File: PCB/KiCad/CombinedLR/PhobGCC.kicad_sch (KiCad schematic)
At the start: 66 parts, among them J1 Conn_01x06_Female, J2 Conn_01x04_Female, J3 Conn_01x01_Male, J5 Conn_01x02_Male, Q1 Q_NMOS_GSD, Q2 Q_PMOS_GDS, Q3 Q_NMOS_GSD, SW1 A, SW10 Dup, SW11 Dright, SW12 Ddown, SW2 B, SW3 X, SW4 Y, SW5 Start, SW6 L, SW7 R, SW9 Dleft, U1 Teensy4.0, U2 2x DRV5053CAQLPGM Hall Effect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, U3 GP2S60-MFG, U4 GP2S60-MFG

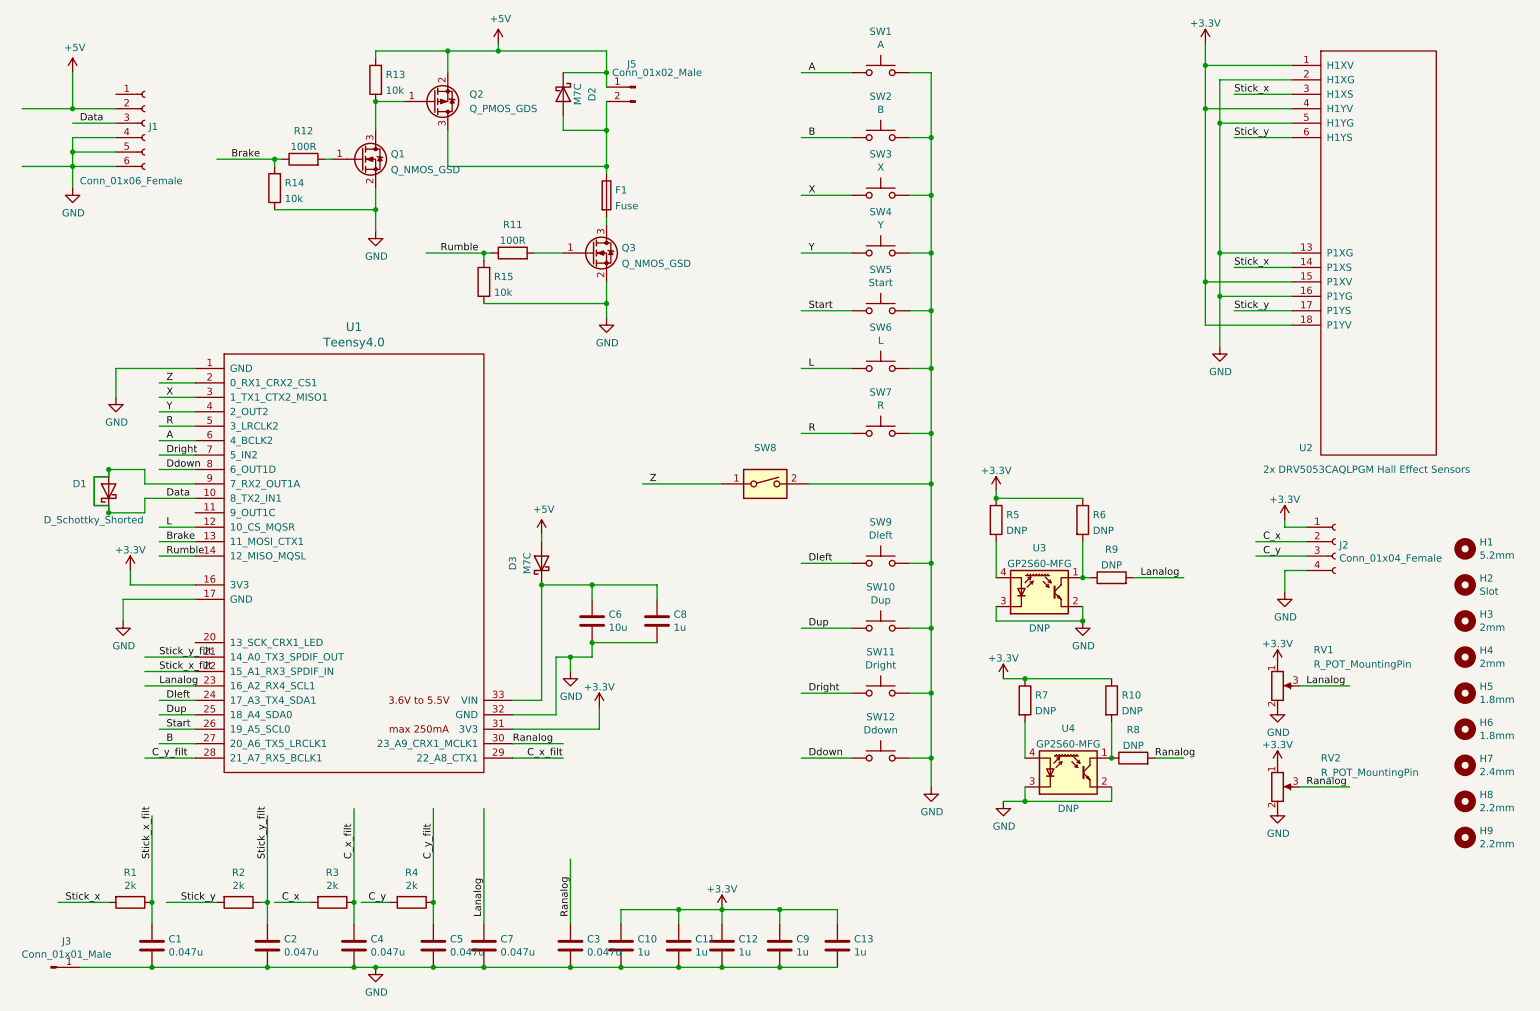
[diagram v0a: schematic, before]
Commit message: Updates
- switched rumble pads to SMD and matched OEM placement.
- aligned both sets of trigger pads to be horizontal for convenience and consistency.
- centered c-stick pins to the board edge.
- rerouted some areas to have a more consistent copper fill.
- fixed trigger board width (switched 7.5mm to 7.35mm).
- increased dpad button pad size to make for easier hand soldering.
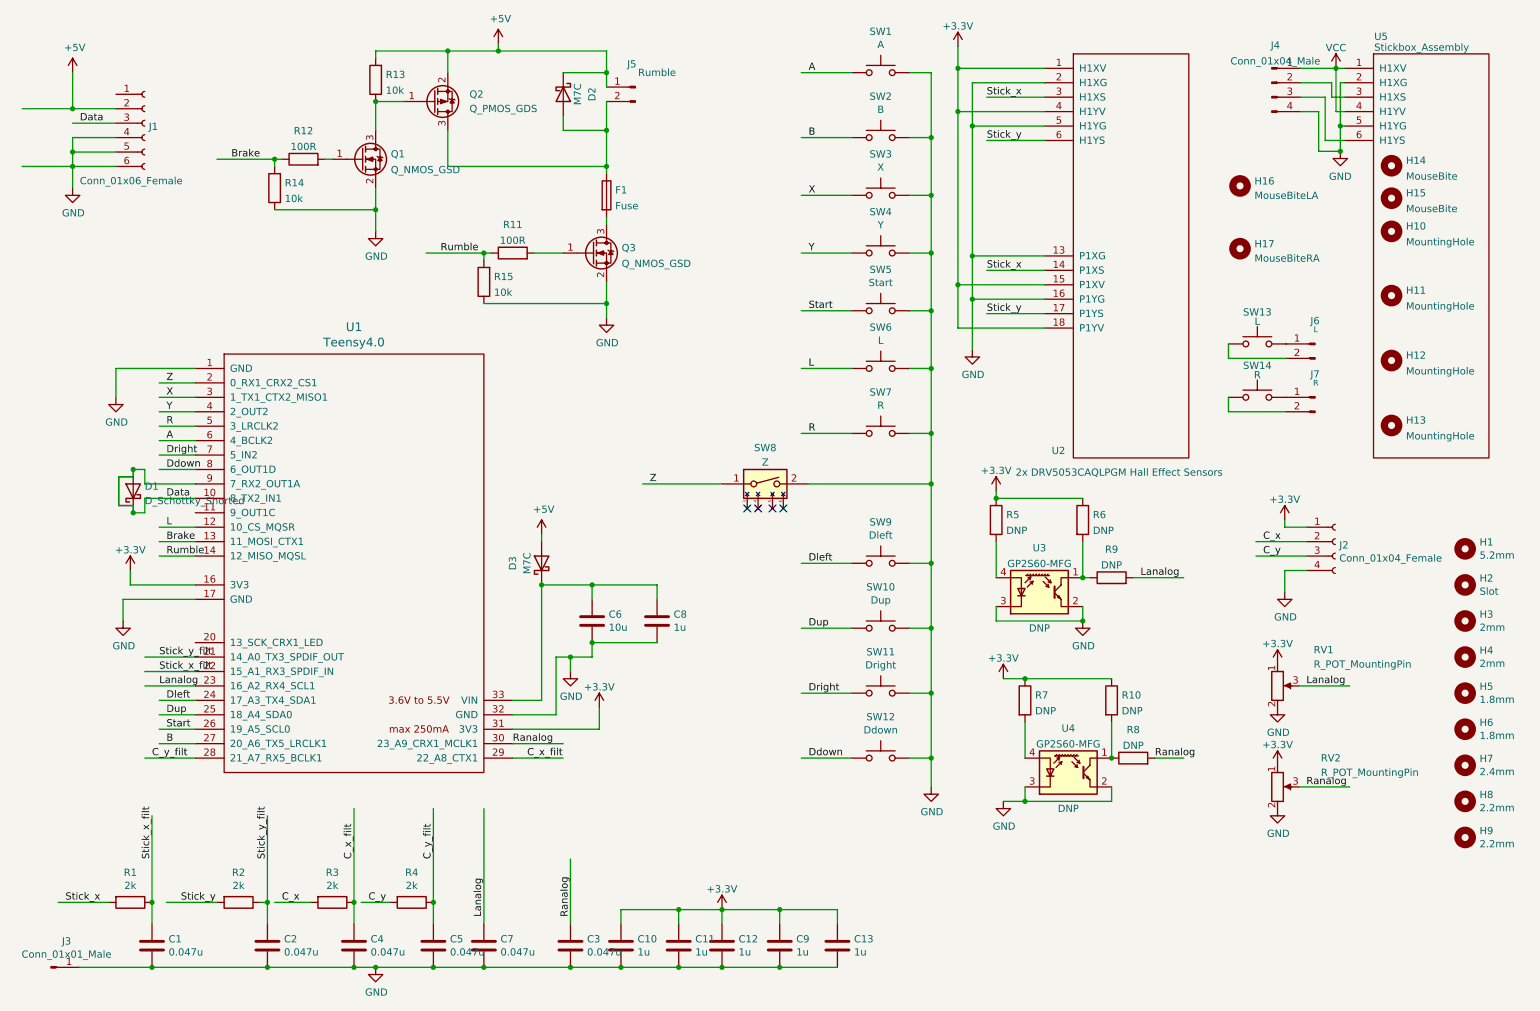
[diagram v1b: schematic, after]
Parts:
- removed D1: D_Schottky_Shorted, PhobGCC_Footprints:D_SOD-523_Shorted, symbol Gamecube MB:D_Schottky_Shorted
- added D1: D_Schottky_Shorted, wavbrd:D_SOD-523_Shorted, symbol PhobGCC_Symbol_Library:D_Schottky_Shorted
- added H10: MountingHole, PhobGCC_Footprints:MountingHole_1.8mm, symbol Mechanical:MountingHole
- added H11: MountingHole, PhobGCC_Footprints:MountingHole_5.2mm, symbol Mechanical:MountingHole
- added H12, H13: MountingHole, PhobGCC_Footprints:MountingHole_2.0mm, symbol Mechanical:MountingHole
- added H14, H15: MouseBite, PhobGCC_Footprints:breakaway-mousebites-double, symbol Mechanical:MountingHole
- added H16: MouseBiteLA, PhobGCC_Footprints:breakaway-mousebites-double, symbol Mechanical:MountingHole
- added H17: MouseBiteRA, PhobGCC_Footprints:breakaway-mousebites-double, symbol Mechanical:MountingHole
- added J4: Conn_01x04_Male, Connector_PinHeader_2.00mm:PinHeader_1x04_P2.00mm_Vertical, symbol Connector:Conn_01x04_Male
- added J6: L, PhobGCC_Footprints:Pin_Header_Straight_1x02_Pitch2.54mm, symbol Connector:Conn_01x02_Male
- added J7: R, PhobGCC_Footprints:Pin_Header_Straight_1x02_Pitch2.54mm, symbol Connector:Conn_01x02_Male
- added SW13: L, PhobGCC_Footprints:Trigger_Contact, symbol Switch:SW_Push
- added SW14: R, PhobGCC_Footprints:Trigger_Contact, symbol Switch:SW_Push
- added U5: Stickbox_Assembly, PhobGCC_Footprints:GCC_Stickbox_Hall_Only, symbol Gamecube MB:Stickbox_Assembly_Hall_Only
- J5: value Conn_01x02_Male -> Rumble; footprint PhobGCC_Footprints:Pin_Header_Straight_1x02_Pitch2.54mm -> (none)
- SW8: value (none) -> Z; symbol Switch:SW_DIP_x01 -> PhobGCC_Symbol_Library:SW_DIP_x01
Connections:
- net Data: now also D1.1 (K), D1.2 (A)
- net GND: now also J4.4 (Pin_4), U5.2 (H1XG), U5.5 (H1YG)
- new net: J6.1 (Pin_1), SW13.1
- new net: J6.2 (Pin_2), SW13.2
- new net: J7.1 (Pin_1), SW14.1
- new net: J7.2 (Pin_2), SW14.2
- new net: J4.2 (Pin_2), U5.3 (H1XS)
- new net: J4.3 (Pin_3), U5.6 (H1YS)
- new net VCC: J4.1 (Pin_1), U5.1 (H1XV), U5.4 (H1YV)
- no-connect marks 0 -> 4
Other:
- moved on the sheet: U2

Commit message: Consolidated footprints to PhobGCC library
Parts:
- C1, C2, C3, C4, C5, C6, C7: footprint Capacitors_SMD:C_0603_HandSoldering -> (none)
- C10, C11, C12, C13, C8, C9: footprint Capacitor_SMD:C_0603_1608Metric_Pad1.08x0.95mm_HandSolder -> (none)
- D1: footprint wavbrd:D_SOD-523_Shorted -> (none)
- D2, D3: footprint Diode_SMD:D_SOD-123 -> (none)
- F1: footprint Resistor_SMD:R_1206_3216Metric -> (none)
- J2: footprint Pin_Headers:Pin_Header_Straight_1x04_Pitch2.00mm -> (none)
- J3: footprint Connector_PinHeader_2.54mm:PinHeader_1x01_P2.54mm_Vertical -> (none)
- J4: footprint Connector_PinHeader_2.00mm:PinHeader_1x04_P2.00mm_Vertical -> (none)
- J5: footprint (none) -> PhobGCC_Footprints:rumble_pins
- Q1, Q2, Q3: footprint Package_TO_SOT_SMD:SOT-23 -> (none)
- R1, R10, R11, R12, R13, R14, R15, R2, R3, R4, R5, R6, R7, R8, R9: footprint Resistor_SMD:R_0603_1608Metric_Pad0.98x0.95mm_HandSolder -> (none)
- RV1: footprint PhobGCC_Footprints:GCC_Slider -> (none)

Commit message: 1.2.3 changes
omron tactile z support, larger c stick pin holes, relocated C10 from underneath button pad
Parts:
- C1, C2, C3, C4, C5, C6, C7: footprint (none) -> PhobGCC_Footprints:C_0603_HandSoldering
- C10, C11, C12, C13, C8, C9: footprint (none) -> PhobGCC_Footprints:C_0603_1608Metric_Pad1.08x0.95mm_HandSolder
- D1: footprint (none) -> PhobGCC_Footprints:D_SOD-523_Shorted
- D2, D3: footprint (none) -> PhobGCC_Footprints:D_SOD-123
- F1: footprint (none) -> PhobGCC_Footprints:Fuse_1206_3216Metric
- J2, J4: footprint (none) -> PhobGCC_Footprints:PinHeader_1x04_P2.00mm_Vertical
- J3: footprint (none) -> PhobGCC_Footprints:PinHeader_1x01_P2.54mm_Vertical
- Q1, Q2, Q3: footprint (none) -> PhobGCC_Footprints:SOT-23
- R1, R11, R12, R13, R14, R15, R2, R3, R4: footprint (none) -> PhobGCC_Footprints:R_0603_1608Metric_Pad0.98x0.95mm_HandSolder
- R10, R5, R6, R7, R8, R9: footprint (none) -> PhobGCC_Footprints:R_0603_1608_DNP
- RV1: footprint (none) -> PhobGCC_Footprints:GCC_Slider
- SW8: footprint PhobGCC_Footprints:Z_Switch_Edge -> (none)
